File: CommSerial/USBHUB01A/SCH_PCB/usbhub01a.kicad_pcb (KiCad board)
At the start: 4 copper layers, 80.8 x 80.8 mm, 149 parts, among them CON1 BARREL_JACK, J1 JUMP_2x1, J10 JUMP_2x1, J11 JUMP_2x1, J12 JUMP_5X2, J13 USB3_A, J14 USB3_B, J15 USB3_A, J16 USB3_A, J17 USB3_A, J18 JUMP_3X2, J2 JUMP_2x1, J3 JUMP_2x1, J4 JUMP_2x1, J5 JUMP_2x1, J6 JUMP_2x1, J7 JUMP_2x1, J8 JUMP_2x1, J9 JUMP_2x1, M1 HOLE, M2 HOLE, M3 HOLE, M4 HOLE, SW1 SPST, U1 CAT24C04YI-GT3OSCT-ND, U2 TUSB8041IPAPRQ1, U3 TPS7A4533KTTR, U4 TPS74801RGWR, U5 TPS2001CDGN, U6 TPS2001CDGN, U7 TPS2001CDGN, U8 TPS2001CDGN, Y1 24MHz

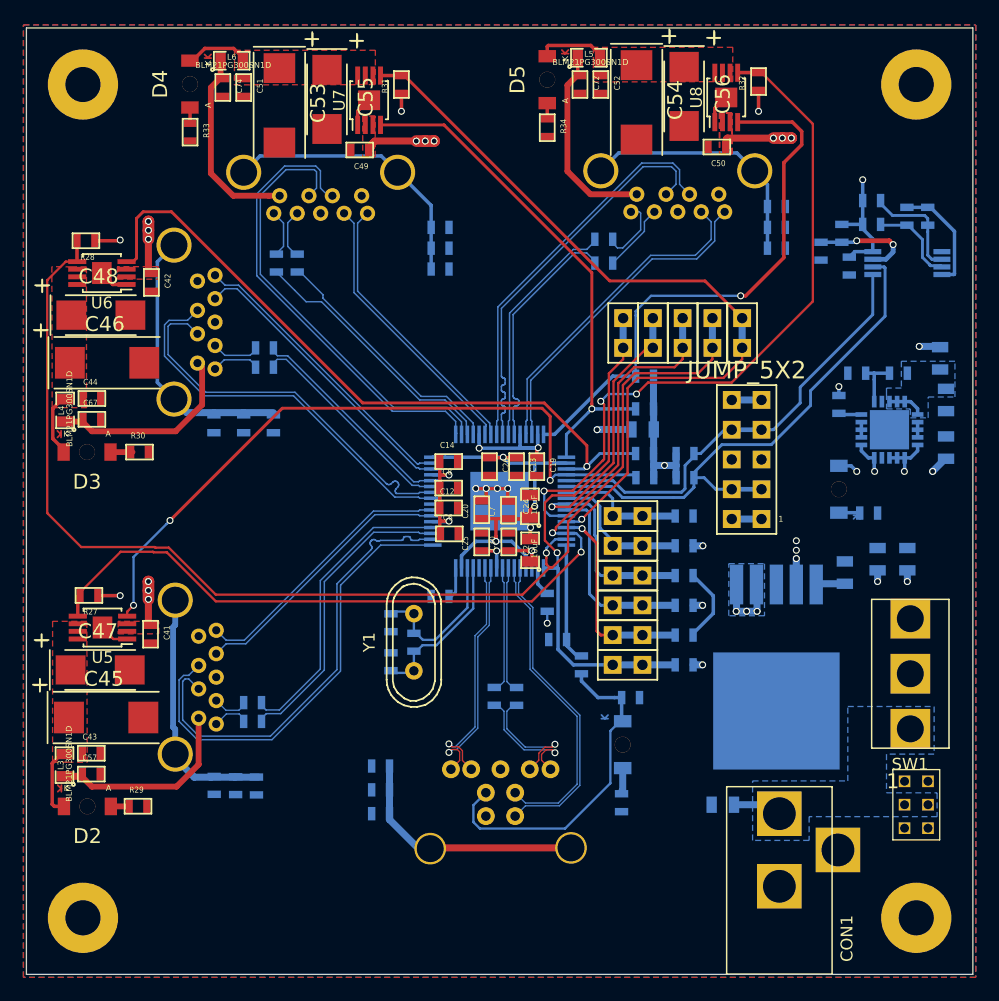
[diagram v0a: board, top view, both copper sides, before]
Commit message: Délka differenciálních párů přispůsobená ručne.
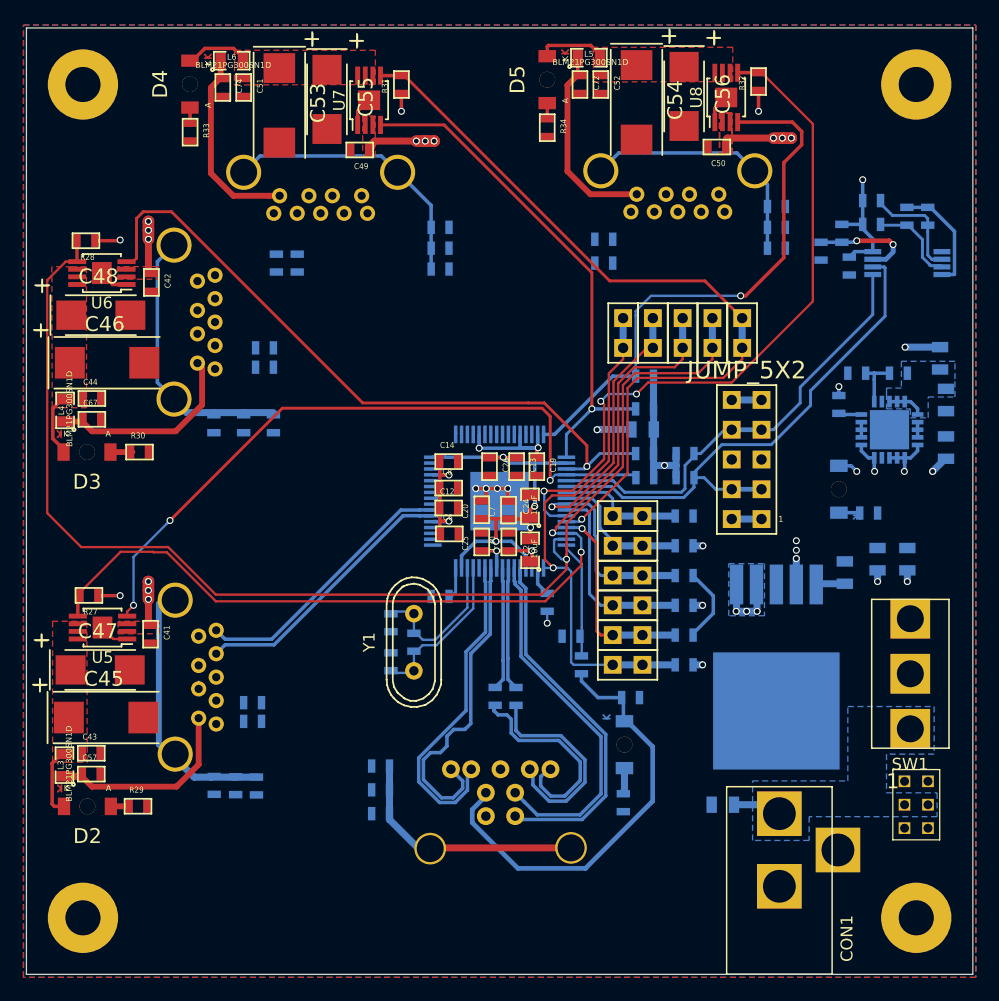
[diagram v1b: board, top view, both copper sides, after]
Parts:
- moved R17 1.18 mm to (153.4, 113.1)
- moved D6 0.15 mm to (158.0, 122.4)
- moved R37 0.15 mm to (157.9, 127.3)
- moved C63 0.08 mm to (146.9, 118.3)
- moved C64 0.05 mm to (148.7, 118.3)
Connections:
- C59 pad 1: /USB_SSTXM_DN1+ -> /USB_SSTXM_DN1-
- C60 pad 1: /USB_SSTXM_DN1- -> /USB_SSTXM_DN1+
- C63 pad 1: /USB_SSTXM_UP+ -> /USB_SSTXM_UP-
- C64 pad 1: /USB_SSTXM_UP- -> /USB_SSTXM_UP+
- C69 pad 1: /USB_SSTXM_DN2+ -> /USB_SSTXM_DN2-
- C70 pad 1: /USB_SSTXM_DN2- -> /USB_SSTXM_DN2+
- C76 pad 1: /USB_SSTXM_DN4+ -> /USB_SSTXM_DN4-
- C77 pad 1: /USB_SSTXM_DN4- -> /USB_SSTXM_DN4+
- C79 pad 1: /USB_SSTXM_DN3+ -> /USB_SSTXM_DN3-
- C80 pad 1: /USB_SSTXM_DN3- -> /USB_SSTXM_DN3+
- J13 pad 2: /USB_DM_DN1+ -> /USB_DM_DN1-
- J13 pad 3: /USB_DM_DN1- -> /USB_DM_DN1+
- J13 pad 5: /USB_SSRXM_DN1+ -> /USB_SSRXM_DN1-
- J13 pad 6: /USB_SSRXM_DN1- -> /USB_SSRXM_DN1+
- J14 pad 2: /USB_DM_UP+ -> /USB_DM_UP-
- J14 pad 3: /USB_DM_UP- -> /USB_DM_UP+
- J14 pad 8: /USB_SSRXM_UP+ -> /USB_SSRXM_UP-
- J14 pad 9: /USB_SSRXM_UP- -> /USB_SSRXM_UP+
- J15 pad 2: /USB_DM_DN2+ -> /USB_DM_DN2-
- J15 pad 3: /USB_DM_DN2- -> /USB_DM_DN2+
- J15 pad 5: /USB_SSRXM_DN2+ -> /USB_SSRXM_DN2-
- J15 pad 6: /USB_SSRXM_DN2- -> /USB_SSRXM_DN2+
- J16 pad 2: /USB_DM_DN4+ -> /USB_DM_DN4-
- J16 pad 3: /USB_DM_DN4- -> /USB_DM_DN4+
- J16 pad 5: /USB_SSRXM_DN4+ -> /USB_SSRXM_DN4-
- J16 pad 6: /USB_SSRXM_DN4- -> /USB_SSRXM_DN4+
- J17 pad 2: /USB_DM_DN3+ -> /USB_DM_DN3-
- J17 pad 3: /USB_DM_DN3- -> /USB_DM_DN3+
- J17 pad 5: /USB_SSRXM_DN3+ -> /USB_SSRXM_DN3-
- J17 pad 6: /USB_SSRXM_DN3- -> /USB_SSRXM_DN3+
- U2 pad 21: /USB_DM_UP- -> /USB_DM_UP+
- U2 pad 22: /USB_DM_UP+ -> /USB_DM_UP-
- U2 pad 23: /USB_SSTXM_UP- -> /USB_SSTXM_UP+
- U2 pad 24: /USB_SSTXM_UP+ -> /USB_SSTXM_UP-
- U2 pad 26: /USB_SSRXM_UP- -> /USB_SSRXM_UP+
- U2 pad 27: /USB_SSRXM_UP+ -> /USB_SSRXM_UP-
- U2 pad 33: /USB_DM_DN1- -> /USB_DM_DN1+
- U2 pad 34: /USB_DM_DN1+ -> /USB_DM_DN1-
- U2 pad 35: /USB_SSTXM_DN1- -> /USB_SSTXM_DN1+
- U2 pad 36: /USB_SSTXM_DN1+ -> /USB_SSTXM_DN1-
- U2 pad 38: /USB_SSRXM_DN1- -> /USB_SSRXM_DN1+
- U2 pad 39: /USB_SSRXM_DN1+ -> /USB_SSRXM_DN1-
- U2 pad 41: /USB_DM_DN2- -> /USB_DM_DN2+
- U2 pad 42: /USB_DM_DN2+ -> /USB_DM_DN2-
- U2 pad 43: /USB_SSTXM_DN2- -> /USB_SSTXM_DN2+
- U2 pad 44: /USB_SSTXM_DN2+ -> /USB_SSTXM_DN2-
- U2 pad 46: /USB_SSRXM_DN2- -> /USB_SSRXM_DN2+
- U2 pad 47: /USB_SSRXM_DN2+ -> /USB_SSRXM_DN2-
- U2 pad 49: /USB_DM_DN3- -> /USB_DM_DN3+
- U2 pad 50: /USB_DM_DN3+ -> /USB_DM_DN3-
- U2 pad 51: /USB_SSTXM_DN3- -> /USB_SSTXM_DN3+
- U2 pad 52: /USB_SSTXM_DN3+ -> /USB_SSTXM_DN3-
- U2 pad 54: /USB_SSRXM_DN3- -> /USB_SSRXM_DN3+
- U2 pad 55: /USB_SSRXM_DN3+ -> /USB_SSRXM_DN3-
- U2 pad 56: /USB_DM_DN4- -> /USB_DM_DN4+
- U2 pad 57: /USB_DM_DN4+ -> /USB_DM_DN4-
- U2 pad 58: /USB_SSTXM_DN4- -> /USB_SSTXM_DN4+
- U2 pad 59: /USB_SSTXM_DN4+ -> /USB_SSTXM_DN4-
- U2 pad 61: /USB_SSRXM_DN4- -> /USB_SSRXM_DN4+
- U2 pad 62: /USB_SSRXM_DN4+ -> /USB_SSRXM_DN4-
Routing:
- net /USB_DM_DN1+: track 39.2 -> 0.00 mm
- net /USB_DM_DN3-: track 39.8 -> 0.76 mm
- net /USB_DM_DN1-: track 39.2 -> 0.56 mm
- net /USB_DM_DN3+: track 38.4 -> 1.15 mm
- net /USB_DM_DN4+: track 34.3 -> 0.00 mm
- net /USB_DM_DN4-: track 34.2 -> 0.00 mm
- net /USB_DM_DN2-: track 34.1 -> 0.12 mm
- net /USB_DM_DN2+: track 34.0 -> 0.19 mm
- net /USB_SSRXM_DN4+: track 28.8 -> 0.17 mm
- net /USB_SSRXM_DN4-: track 28.3 -> 0.64 mm
- net /USB_SSTXM_DN1-: track 26.3 -> 0.43 mm
- net /USB_SSTXM_DN1+: track 26.1 -> 0.61 mm
- net /USB_SSRXM_DN2-: track 25.5 -> 0.12 mm
- net /USB_SSRXM_DN2+: track 25.4 -> 0.19 mm
- net /USB_SSRXM_DN3-: track 24.5 -> 0.85 mm
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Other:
- net class Default: clearance 0.2 -> 0.001
- rule trace_clearance: 0.2 -> 0.001
- rule trace_min: 0.11176 -> 0.1

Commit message: První verze hotového layoutu
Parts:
- moved C79 0.31 mm to (130.3, 81.1)
- moved C80 0.31 mm to (128.5, 81.1)
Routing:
- net /USB_DM_DN1+: track 0.00 -> 41.3 mm
- net /USB_DM_DN1-: track 0.56 -> 41.4 mm
- net /USB_DM_DN3-: track 0.76 -> 40.6 mm
- net /USB_DM_DN3+: track 1.15 -> 41.0 mm
- net /USB_DM_DN4+: track 0.00 -> 34.3 mm
- net /USB_DM_DN4-: track 0.00 -> 34.3 mm
- net /USB_DM_DN2-: track 0.12 -> 33.4 mm
- net /USB_DM_DN2+: track 0.19 -> 33.5 mm
- net /USB_SSRXM_DN4+: track 0.17 -> 28.7 mm
- net /USB_SSRXM_DN4-: track 0.64 -> 28.8 mm
- net /USB_SSRXM_DN2+: track 0.19 -> 25.5 mm
- net /USB_SSRXM_DN2-: track 0.12 -> 25.4 mm
- net /USB_SSTXM_DN1+: track 0.61 -> 25.4 mm
- net /USB_SSTXM_DN1-: track 0.43 -> 25.2 mm
- net /USB_SSRXM_DN3+: track 1.32 -> 25.3 mm
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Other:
- net class Default: clearance 0.001 -> 0.1
- rule trace_clearance: 0.001 -> 0.1

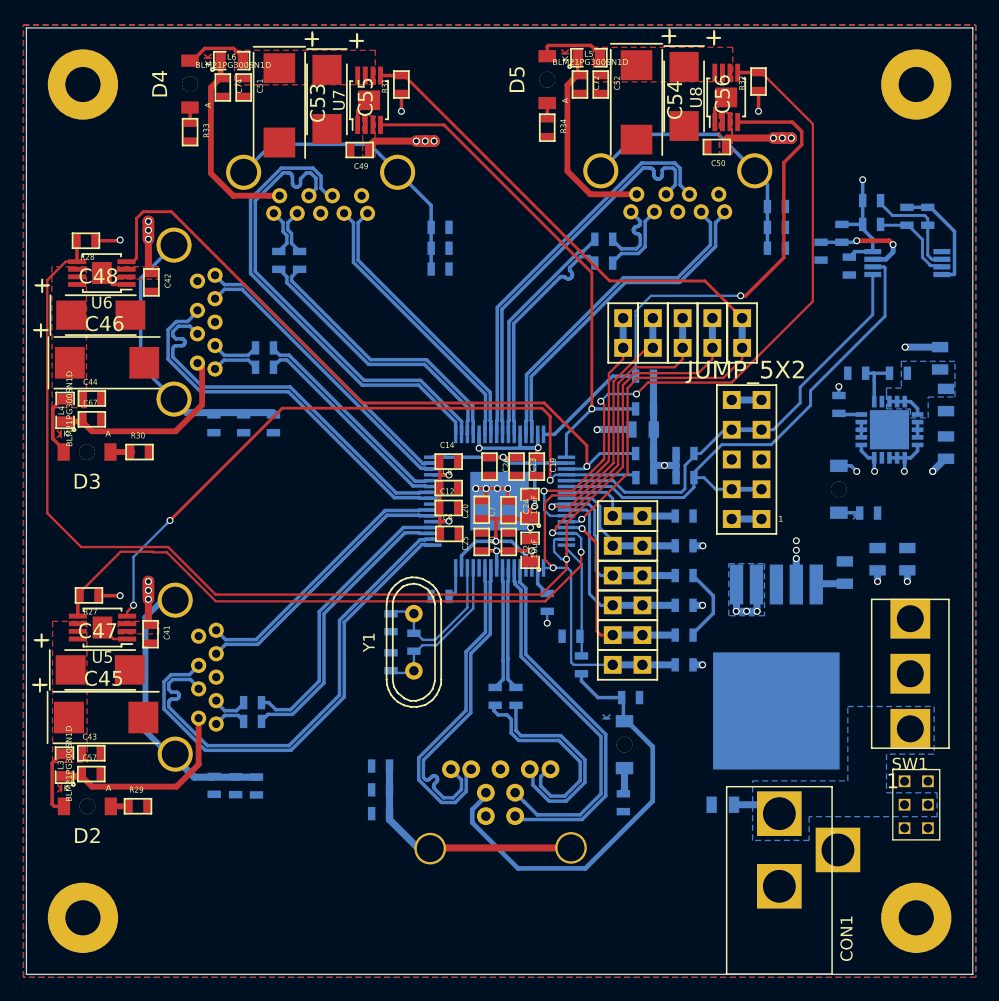
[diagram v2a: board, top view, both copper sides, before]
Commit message: Změna rozměrů diff. párů
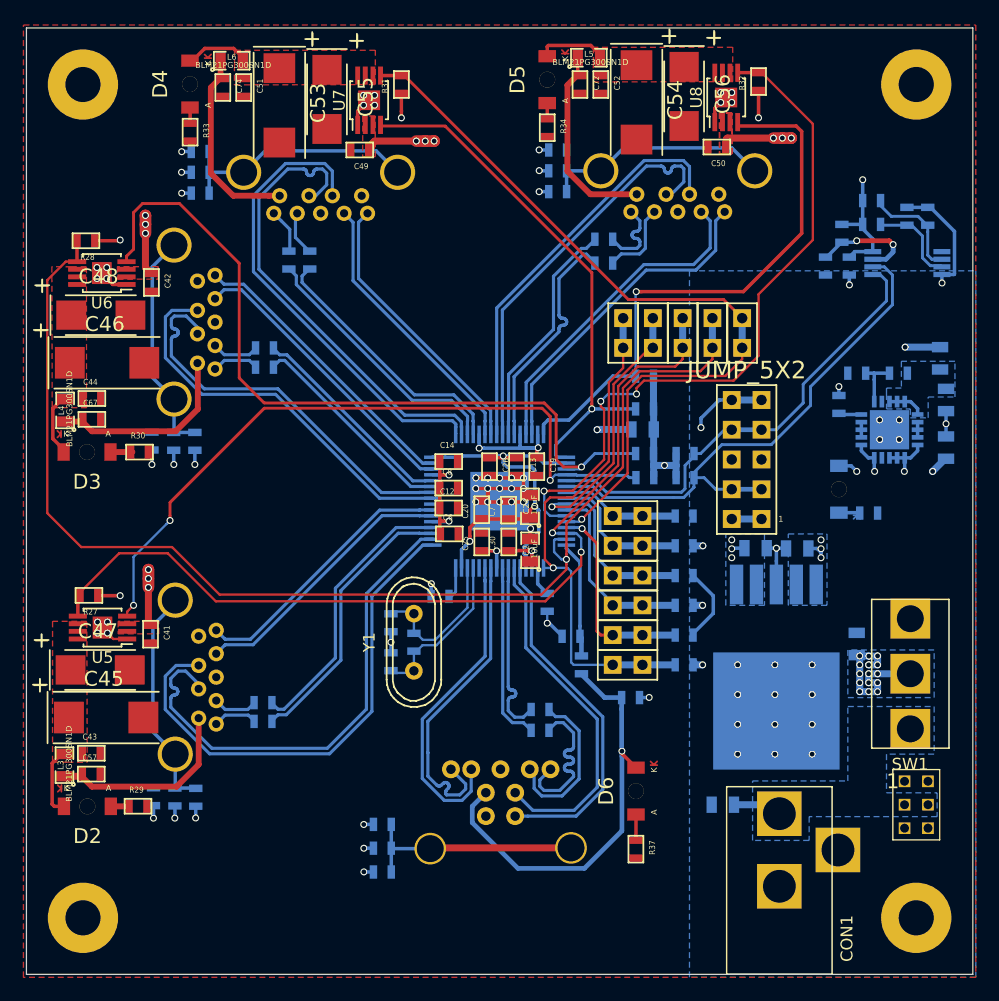
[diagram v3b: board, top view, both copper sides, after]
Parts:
- C65: value 1nF -> 1nF 2kV
- D6, R37: moved to F.Cu
- moved C75 22.8 mm to (121.8, 71.8), turned to 180 degrees
- moved C81 21.5 mm to (121.8, 73.5), turned to 180 degrees
- moved R40 20.7 mm to (121.8, 75.3), turned to 180 degrees
- moved C73 20.5 mm to (152.3, 71.6), turned to 180 degrees
- moved C78 19.3 mm to (152.3, 73.4), turned to 180 degrees
- moved R39 18.7 mm to (152.3, 75.2), turned to 180 degrees
- moved C36 10.5 mm to (169.2, 105.6), turned to 0 degrees
- moved C37 8.43 mm to (177.8, 113.8)
- moved C71 6.87 mm to (121.3, 96.5)
- moved C68 6.15 mm to (119.5, 96.5)
- moved R38 5.48 mm to (117.7, 96.5)
- moved C61 5.27 mm to (121.4, 126.9)
- moved C58 5.27 mm to (117.8, 126.8)
- moved R35 5.27 mm to (119.6, 126.8)
- moved R36 4.98 mm to (137.3, 129.2)
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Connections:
- C38 pad 1: Net-(C38-Pad1) -> +3V3
- U1 pad 1: (no net) -> Net-(U1-Pad1)
- U2 pad 28: (no net) -> Net-(U2-Pad28)
- U2 pad 40: (no net) -> Net-(U2-Pad40)
- U3 pad 5: Net-(C38-Pad1) -> +3V3
- U4 pad 17: (no net) -> Net-(U4-Pad17)
- U4 pad 21: GND -> (no net)
- U4 pad 9: (no net) -> Net-(U4-Pad9)
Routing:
- net GND: track 39.1 -> 122.1 mm, vias 7 -> 69
- net +5V: track 32.0 -> 58.2 mm, vias 17 -> 30
- net /PWRON2_BATEN2: track 59.6 -> 66.8 mm
- net /USB_SSTXM_UP-: track 11.0 -> 15.5 mm
- net /USB_SSTXM_UP+: track 11.1 -> 15.6 mm
- net /USBPORT/SSTX_N: track 18.5 -> 14.2 mm
- net /USBPORT/SSTX_P: track 18.5 -> 14.3 mm
- net /IO3V3: track 46.1 -> 49.7 mm
- net Net-(C75-Pad1): track 24.5 -> 21.2 mm
- net Net-(C68-Pad1): track 24.5 -> 21.2 mm
- net /USB_DM_DN1-: track 41.4 -> 44.3 mm
- net /USB_VBUS_UP: track 37.3 -> 39.8 mm, vias 0 -> 1
- net Net-(C38-Pad1): track 2.47 -> 0.00 mm
- net /USB_DM_DN1+: track 41.3 -> 43.6 mm
- net /SDA: track 38.6 -> 40.1 mm
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- added copper zone on B.Cu, net +3V3
- added copper zone on In1.Cu, net GND
- added copper zone on In1.Cu, net Net-(C35-Pad1)
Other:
- net class Default: clearance 0.1 -> 0.2
- rule trace_clearance: 0.1 -> 0.2

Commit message: Uprava blokovaní a smd krystal
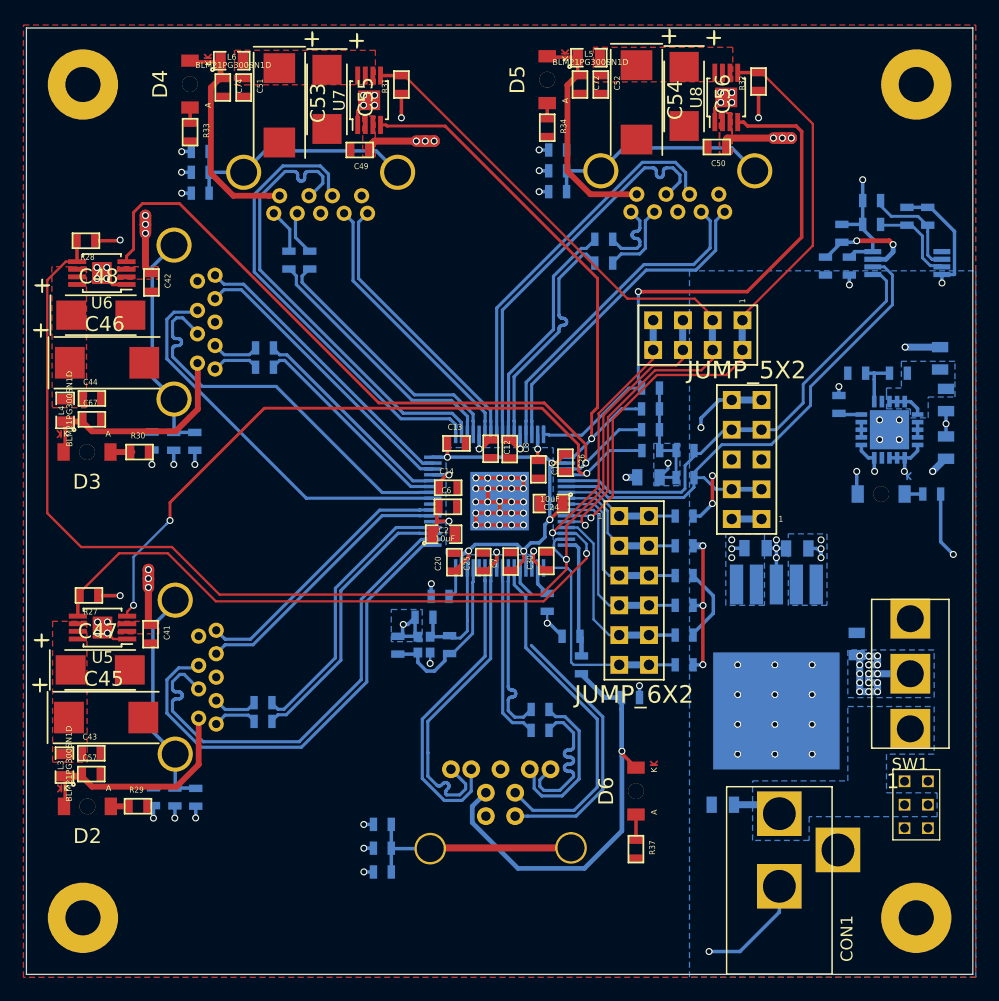
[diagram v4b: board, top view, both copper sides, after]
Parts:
- removed J10, J11, J3, J4, J5, J6, J7, J8, J9: JUMP_2x1, Mlab_Pin_Headers:Straight_2x01
- J1: footprint Mlab_Pin_Headers:Straight_2x01 -> Mlab_Pin_Headers:Straight_2x04
- J2: value JUMP_2x1 -> JUMP_6X2; footprint Mlab_Pin_Headers:Straight_2x01 -> Mlab_Pin_Headers:Straight_2x06
- Y1: footprint Crystals:Crystal_HC49-U_Vertical -> Crystals:NX2016HA; moved to B.Cu
- moved J2 22.0 mm to (158.8, 109.2), turned to 0 degrees
- moved C2 7.51 mm to (142.5, 104.4), turned to 0 degrees
- moved C26 6.49 mm to (152.9, 98.3)
- moved J1 6.38 mm to (164.2, 87.4), turned to 270 degrees
- moved C12 6.19 mm to (146.6, 97.1), turned to 270 degrees
- moved C8 6.18 mm to (148.2, 97.2), turned to 270 degrees
- moved R23 5.62 mm to (184.2, 101.0)
- moved C13 5.50 mm to (143.6, 96.7), turned to 0 degrees
- moved C20 5.04 mm to (143.5, 106.8)
- moved C7 4.40 mm to (148.3, 106.8)
- moved L1 4.12 mm to (160.0, 99.6)
- moved D1 3.63 mm to (179.9, 101.0), turned to 0 degrees
- moved C30 3.59 mm to (151.3, 106.7)
- moved R12 3.05 mm to (143.1, 113.8)
- moved C32 2.86 mm to (140.9, 111.5), turned to 180 degrees
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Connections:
- C57 pad 1: Net-(C57-Pad1) -> /VBUS1
- C67 pad 1: Net-(C67-Pad1) -> /VBUS2
- C72 pad 1: Net-(C72-Pad1) -> /VBUS4
- C74 pad 1: Net-(C74-Pad1) -> /VBUS3
- D2 pad 2: /DN1_VBUS -> /VBUS1
- D3 pad 2: /DN2_VBUS -> /VBUS2
- D4 pad 2: /DN3_VBUS -> /VBUS3
- D5 pad 2: /DN4_VBUS -> /VBUS4
- J1 pad 1: /TEST_TRSTZ -> /OVERCUR4Z
- J1 pad 2: /TEST_TRSTZ -> /OVERCUR4Z
- J13 pad 1: Net-(C57-Pad1) -> /VBUS1
- J15 pad 1: Net-(C67-Pad1) -> /VBUS2
- J16 pad 1: Net-(C72-Pad1) -> /VBUS4
- J17 pad 1: Net-(C74-Pad1) -> /VBUS3
- J2 pad 1: /PWRCTL_POL_TDO -> /SMBUSZ_SS_SUS
- J2 pad 2: /PWRCTL_POL_TDO -> /SMBUSZ_SS_SUS
- L3 pad 1: Net-(C57-Pad1) -> /VBUS1
- L4 pad 1: Net-(C67-Pad1) -> /VBUS2
- L5 pad 1: Net-(C72-Pad1) -> /VBUS4
- L6 pad 1: Net-(C74-Pad1) -> /VBUS3
- U1 pad 1: Net-(U1-Pad1) -> (no net)
- U2 pad 28: Net-(U2-Pad28) -> (no net)
- U2 pad 40: Net-(U2-Pad40) -> (no net)
- U4 pad 17: Net-(U4-Pad17) -> (no net)
- U4 pad 21: (no net) -> GND
- U4 pad 9: Net-(U4-Pad9) -> (no net)
- Y1 pad 1: Net-(C31-Pad1) -> Net-(C32-Pad1)
- Y1 pad 2: Net-(C32-Pad1) -> GND
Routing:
- net GND: track 122.1 -> 160.3 mm, vias 69 -> 89
- net /TEST_TRSTZ: track 44.5 -> 19.2 mm, vias 1 -> 0
- net /PWRCTL_POL_TDO: track 36.0 -> 14.6 mm, vias 1 -> 0
- net /VBUS3: track 0.00 -> 19.9 mm
- net /VBUS4: track 0.00 -> 19.7 mm
- net /VBUS1: track 0.00 -> 19.5 mm
- net /VBUS2: track 0.00 -> 19.4 mm
- net Net-(C72-Pad1): track 17.1 -> 0.00 mm
- net Net-(C74-Pad1): track 16.9 -> 0.00 mm
- net Net-(C57-Pad1): track 16.9 -> 0.00 mm
- net Net-(C67-Pad1): track 16.7 -> 0.00 mm
- net /IO1V1: track 67.5 -> 60.9 mm, vias 7 -> 8
- net /DN4_VBUS: track 5.96 -> 0.25 mm
- net /DN1_VBUS: track 5.95 -> 0.25 mm
- net /PWRON2_BATEN2: track 66.8 -> 61.3 mm
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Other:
- rule trace_min: 0.1 -> 0.2
- rule via_min_size: 0.4 -> 0.3
